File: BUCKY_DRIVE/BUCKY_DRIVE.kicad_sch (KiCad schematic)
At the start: 15 parts, among them U2 IFX9201SG_BO, U4 IFX9201SG_BO, U7 IFX9201SG_BO, U9 PCA9548ADB

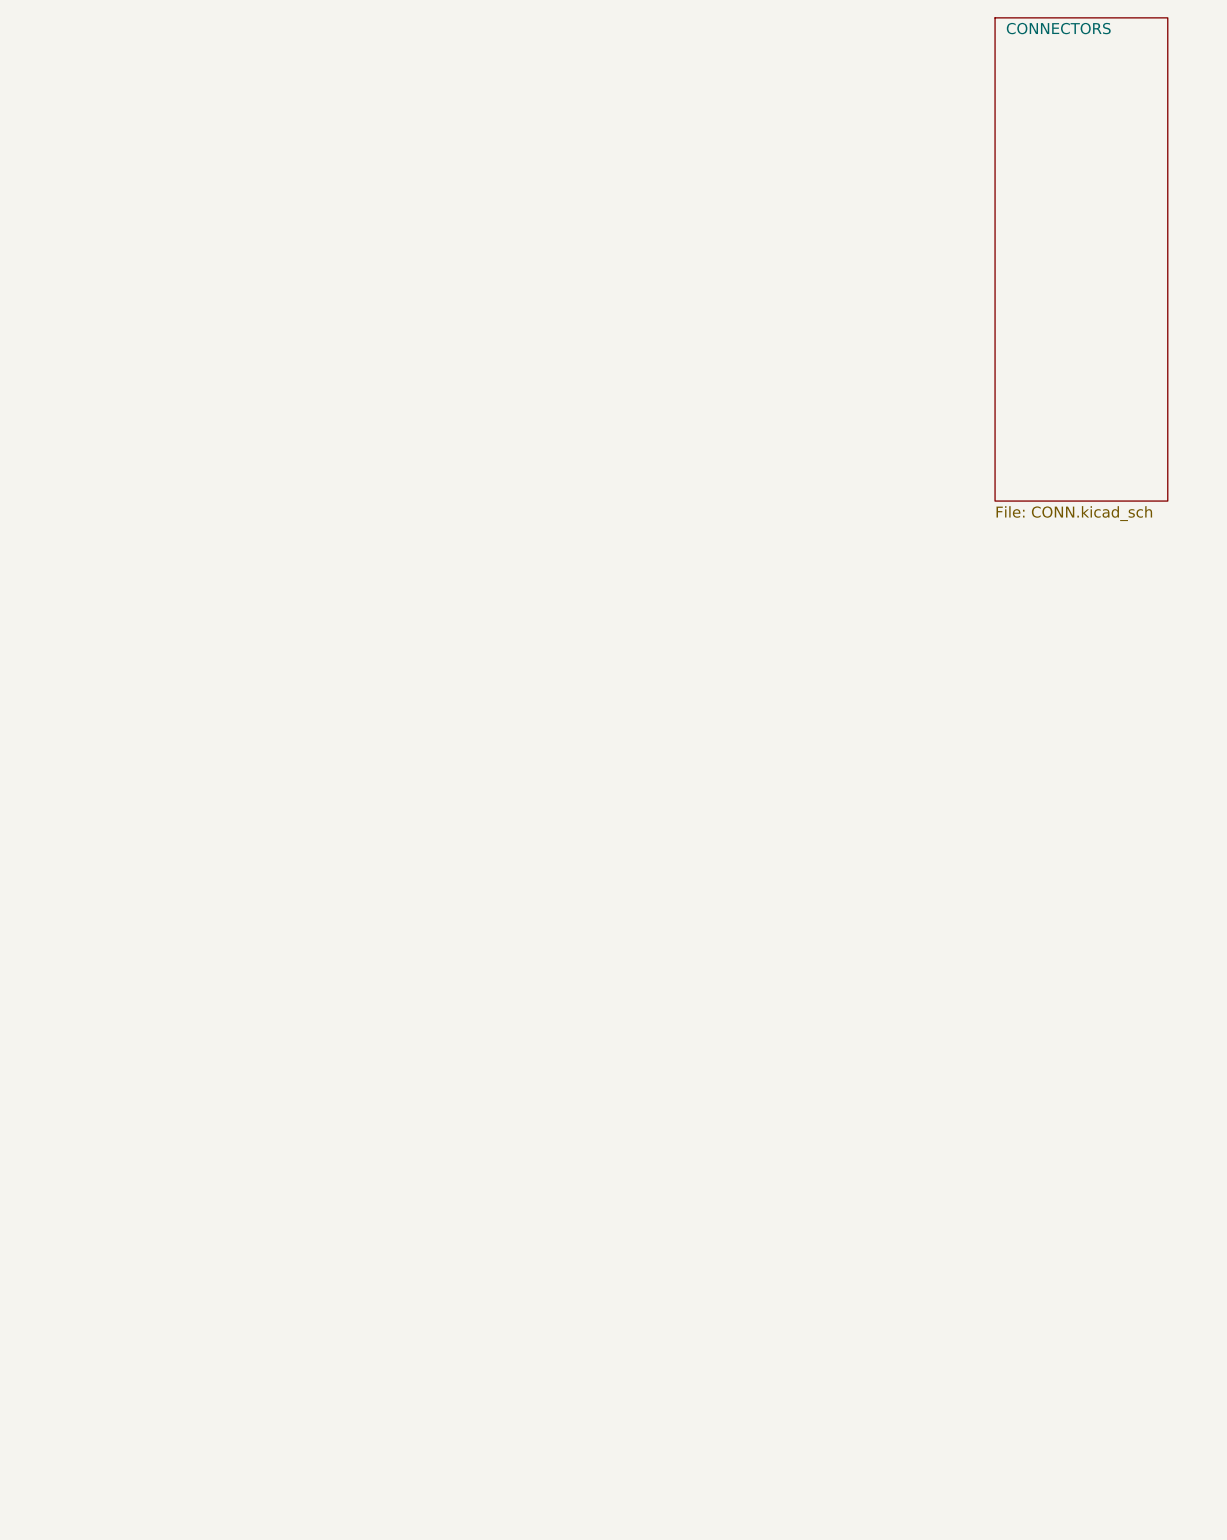
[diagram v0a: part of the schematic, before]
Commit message: chore: start on ldr instead of Q_Photo_N, interrupt instead of analog multiplexer. And a signal for front,back,left,right
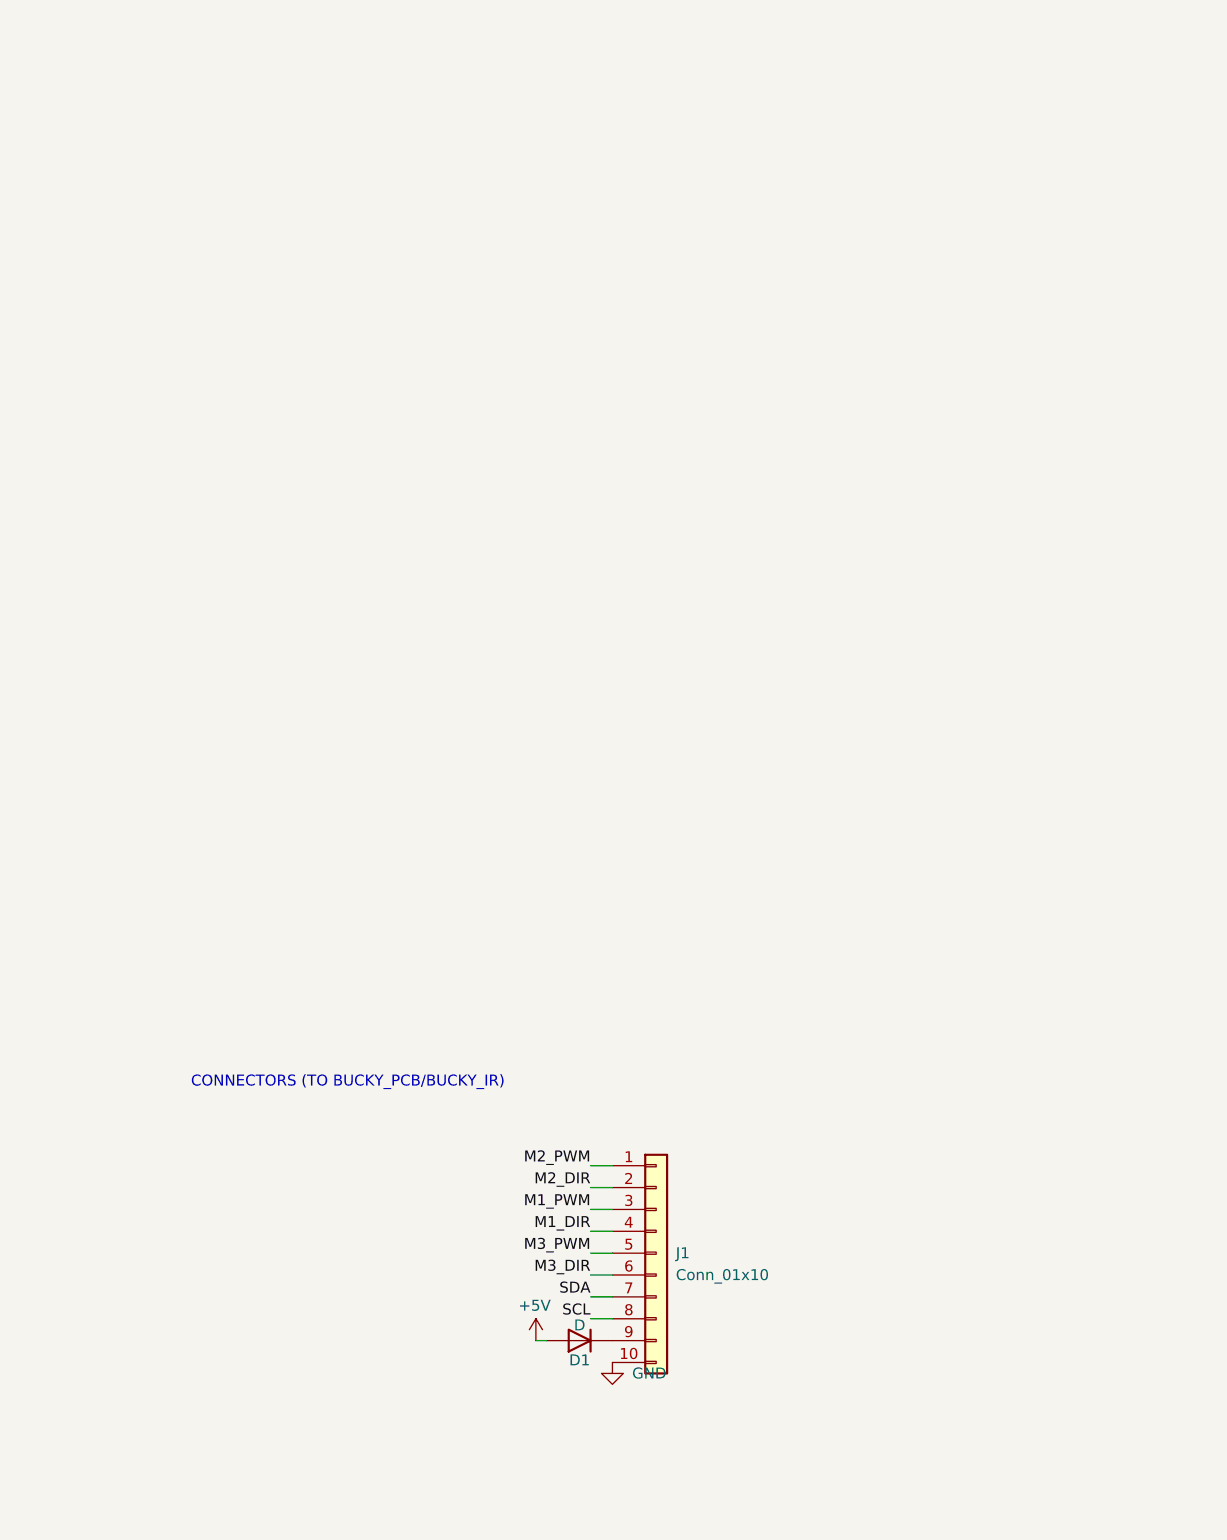
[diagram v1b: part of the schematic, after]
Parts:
- added D1: D, symbol Device:D
- added J1: Conn_01x10, BUCKY_DRIVE:CONN10_S10B-PH_JST, symbol Connector_Generic:Conn_01x10
- U9: footprint DB24 -> BUCKY_DRIVE:DB24
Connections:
- net +5V: now also D1.2 (A)
- net GND: now also J1.10 (Pin_10)
- net M1_DIR: now also J1.4 (Pin_4)
- net M1_PWM: now also J1.3 (Pin_3)
- net M2_DIR: now also J1.2 (Pin_2)
- net M2_PWM: now also J1.1 (Pin_1)
- net M3_DIR: now also J1.6 (Pin_6)
- net M3_PWM: now also J1.5 (Pin_5)
- net SCL: now also J1.8 (Pin_8)
- net SDA: now also J1.7 (Pin_7)
- new net: D1.1 (K), J1.9 (Pin_9)
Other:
- removed sheet CONNECTORS
- note added: "CONNECTORS (TO BUCKY_PCB/BUCKY_IR)"

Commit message: chore: convert 2 layer DRIVE -> 4 layer
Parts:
- D1: footprint (none) -> Diode_SMD:D_0805_2012Metric
- R1, R2, R3, R4, R5, R6: footprint Resistor_SMD:R_0402_1005Metric -> Resistor_SMD:R_0805_2012Metric
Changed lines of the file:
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@@
 			)
 		)
-		(property "Footprint" "Resistor_SMD:R_0402_1005Metric"
+		(property "Footprint" "Resistor_SMD:R_0805_2012Metric"
 			(at 111.76 75.946 90)
 			(effects
@@
 			)
 		)
-		(property "Footprint" "Resistor_SMD:R_0402_1005Metric"
+		(property "Footprint" "Resistor_SMD:R_0805_2012Metric"
 			(at 32.258 74.422 90)
 			(effects
@@
 			)
 		)
-		(property "Footprint" "Resistor_SMD:R_0402_1005Metric"
+		(property "Footprint" "Resistor_SMD:R_0805_2012Metric"
 			(at 39.878 62.484 90)
 			(effects
@@
 			)
 		)
-		(property "Footprint" "Resistor_SMD:R_0402_1005Metric"
+		(property "Footprint" "Resistor_SMD:R_0805_2012Metric"
 			(at 119.634 66.04 90)
 			(effects
@@
 			)
 		)
-		(property "Footprint" "Resistor_SMD:R_0402_1005Metric"
+		(property "Footprint" "Resistor_SMD:R_0805_2012Metric"
 			(at 32.258 71.882 90)
 			(effects
@@
 			)
 		)
-		(property "Footprint" ""
+		(property "Footprint" "Diode_SMD:D_0805_2012Metric"
 			(at 248.92 153.67 0)
 			(effects
@@
 			)
 		)
-		(property "Footprint" "Resistor_SMD:R_0402_1005Metric"
+		(property "Footprint" "Resistor_SMD:R_0805_2012Metric"
 			(at 108.966 66.04 90)
 			(effects

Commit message: fix: BUCKY_MAIN v2?
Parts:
- added D2: D, symbol Device:D
- added J2: Conn_01x01, Connector_PinHeader_2.54mm:PinHeader_1x01_P2.54mm_Vertical, symbol Connector_Generic:Conn_01x01
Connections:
- net +12V: now also D2.2 (A)
- new net: D2.1 (K), J2.1 (Pin_1)
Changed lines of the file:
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@@
 	(wire
 		(pts
+			(xy 210.82 133.35) (xy 214.63 133.35)
+		)
+		(stroke
+			(width 0)
+			(type default)
+		)
+	)
+	(wire
+		(pts
 			(xy 41.656 180.848) (xy 38.862 180.848)
 		)
@@
 	(wire
 		(pts
+			(xy 200.66 133.35) (xy 203.2 133.35)
+		)
+		(stroke
+			(width 0)
+			(type default)
+		)
+	)
+	(wire
+		(pts
 			(xy 41.656 87.884) (xy 44.196 87.884)
 		)
@@
 	)
 	(symbol
+		(lib_id "power:+12V")
+		(at 200.66 133.35 0)
+		(unit 1)
+		(exclude_from_sim no)
+		(in_bom yes)
+		(on_board yes)
+		(dnp no)
+		(property "Reference" "#PWR033"
+			(at 200.66 137.16 0)
+			(effects
+				(font
+					(size 1.27 1.27)
+				)
+				(hide yes)
+			)
+		)
+		(property "Value" "+12V"
+			(at 200.66 129.54 0)
+			(effects
+				(font
+					(size 1.27 1.27)
+				)
+			)
+		)
+		(property "Footprint" ""
+			(at 200.66 133.35 0)
+			(effects
+				(font
+					(size 1.27 1.27)
+				)
+				(hide yes)
+			)
+		)
+		(property "Datasheet" ""
+			(at 200.66 133.35 0)
+			(effects
+				(font
+					(size 1.27 1.27)
+				)
+				(hide yes)
+			)
+		)
+		(property "Description" ""
+			(at 200.66 133.35 0)
+			(effects
+				(font
+					(size 1.27 1.27)
+				)
+				(hide yes)
+			)
+		)
+		(pin "1"
+		)
+		(instances
+			(project "BUCKY_DRIVE"
+				(path "/2d554a70-2f33-463e-9558-83bf87d143ad"
+					(reference "#PWR033")
+					(unit 1)
+				)
+			)
+		)
+	)
+	(symbol
 		(lib_id "Device:R")
 		(at 32.258 72.644 90)
@@
 	)
 	(symbol
+		(lib_id "Device:D")
+		(at 207.01 133.35 180)
+		(unit 1)
+		(exclude_from_sim no)
+		(in_bom yes)
+		(on_board yes)
+		(dnp no)
+		(fields_autoplaced yes)
+		(property "Reference" "D2"
+			(at 207.01 127 0)
+			(effects
+				(font
+					(size 1.27 1.27)
+				)
+			)
+		)
+		(property "Value" "D"
+			(at 207.01 129.54 0)
+			(effects
+				(font
+					(size 1.27 1.27)
+				)
+			)
+		)
+		(property "Footprint" ""
+			(at 207.01 133.35 0)
+			(effects
+				(font
+					(size 1.27 1.27)
+				)
+				(hide yes)
+			)
+		)
+		(property "Datasheet" "~"
+			(at 207.01 133.35 0)
+			(effects
+				(font
+					(size 1.27 1.27)
+				)
+				(hide yes)
+			)
+		)
+		(property "Description" "Diode"
+			(at 207.01 133.35 0)
+			(effects
+				(font
+					(size 1.27 1.27)
+				)
+				(hide yes)
+			)
+		)
+		(property "Sim.Device" "D"
+			(at 207.01 133.35 0)
+			(effects
+				(font
+					(size 1.27 1.27)
+				)
+				(hide yes)
+			)
+		)
+		(property "Sim.Pins" "1=K 2=A"
+			(at 207.01 133.35 0)
+			(effects
+				(font
+					(size 1.27 1.27)
+				)
+				(hide yes)
+			)
+		)
+		(pin "1"
+		)
+		(pin "2"
+		)
+		(instances
+			(project ""
+				(path "/2d554a70-2f33-463e-9558-83bf87d143ad"
+					(reference "D2")
+					(unit 1)
+				)
+			)
+		)
+	)
+	(symbol
 		(lib_id "BUCKY_DRIVE:IFX9201SG_BO")
 		(at 117.856 182.118 0)
@@
 					(unit 1)
 				)
+			)
+		)
+	)
+	(symbol
+		(lib_id "Connector_Generic:Conn_01x01")
+		(at 219.71 133.35 0)
+		(unit 1)
+		(exclude_from_sim no)
+		(in_bom yes)
+		(on_board yes)
+		(dnp no)
+		(fields_autoplaced yes)
+		(property "Reference" "J2"
+			(at 222.25 132.0799 0)
+			(effects
+				(font
+					(size 1.27 1.27)
+				)
+				(justify left)
+			)
+		)
+		(property "Value" "Conn_01x01"
+			(at 222.25 134.6199 0)
+			(effects
+				(font
+					(size 1.27 1.27)
+				)
+				(justify left)
+			)
+		)
+		(property "Footprint" "Connector_PinHeader_2.54mm:PinHeader_1x01_P2.54mm_Vertical"
+			(at 219.71 133.35 0)
+			(effects
+				(font
+					(size 1.27 1.27)
+				)
+				(hide yes)
+			)
+		)
+		(property "Datasheet" "~"
+			(at 219.71 133.35 0)
+			(effects
+				(font
+					(size 1.27 1.27)
+				)
+				(hide yes)
+			)
+		)
+		(property "Description" "Generic connector, single row, 01x01, script generated (kicad-library-utils/schlib/autogen/connector/)"
+			(at 219.71 133.35 0)
+			(effects
+				(font
+					(size 1.27 1.27)
+				)
+				(hide yes)
+			)
+		)
+		(pin "1"
+		)
+		(instances
+			(project ""
+				(path "/2d554a70-2f33-463e-9558-83bf87d143ad"
+					(reference "J2")
+					(unit 1)
+				)
